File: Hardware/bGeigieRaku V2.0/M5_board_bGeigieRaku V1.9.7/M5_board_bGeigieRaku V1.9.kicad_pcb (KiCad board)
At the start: 2 copper layers, 129.4 x 64.6 mm, 27 parts, among them J1 M5 2x15 pin, J10 QI GND, J11 QI charger Plus, J2 Geiger, J3 GPS, J4 Geiger 2, J5 Extra support header, J8 QI charger GND, J9 QI Plus, Q2 IRFR9024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

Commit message: added plates
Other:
- board text added: "screws for the display are M3 12mm"
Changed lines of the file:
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@@
+    (effects (font (size 1.5 1.5) (thickness 0.3)))
+  )
+  (gr_text "screws for the display are M3 12mm" (at 107.7976 167.334) (layer "Eco2.User")
     (effects (font (size 1.5 1.5) (thickness 0.3)))
   )

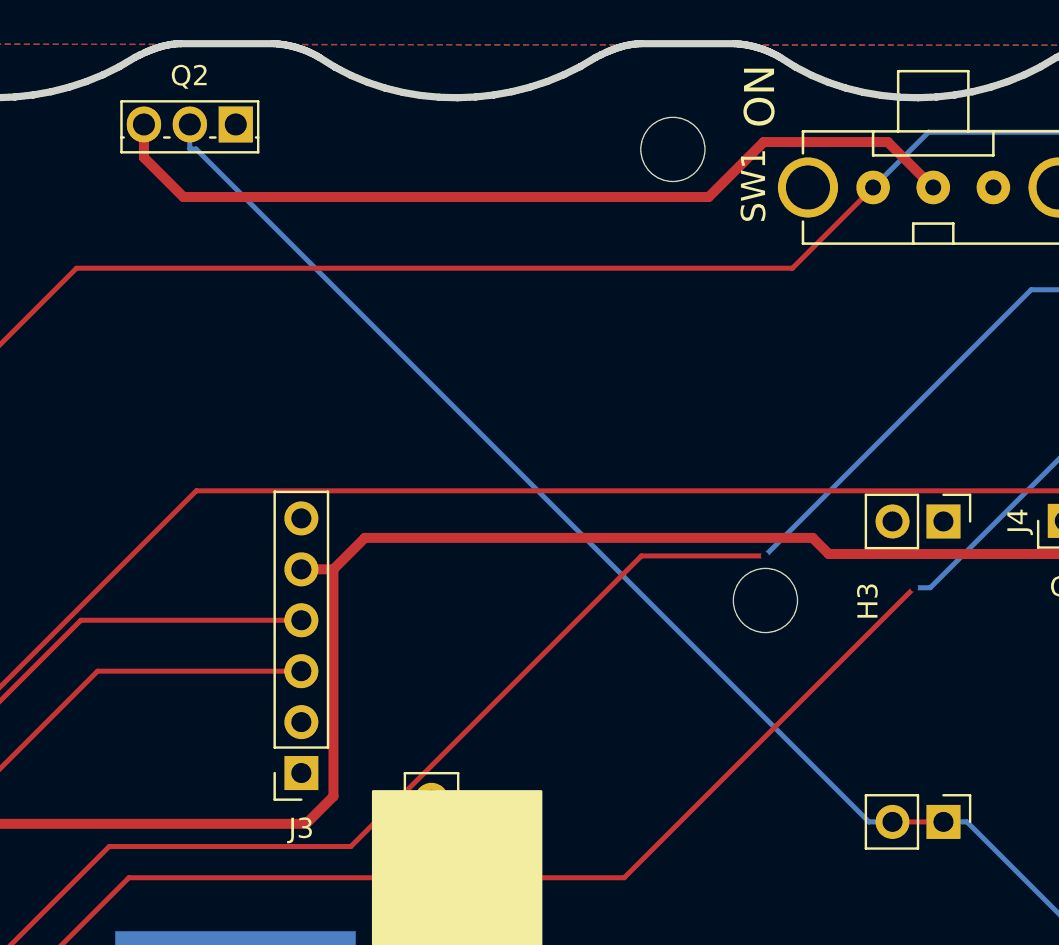
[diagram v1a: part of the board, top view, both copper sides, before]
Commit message: Adde tube rest platform
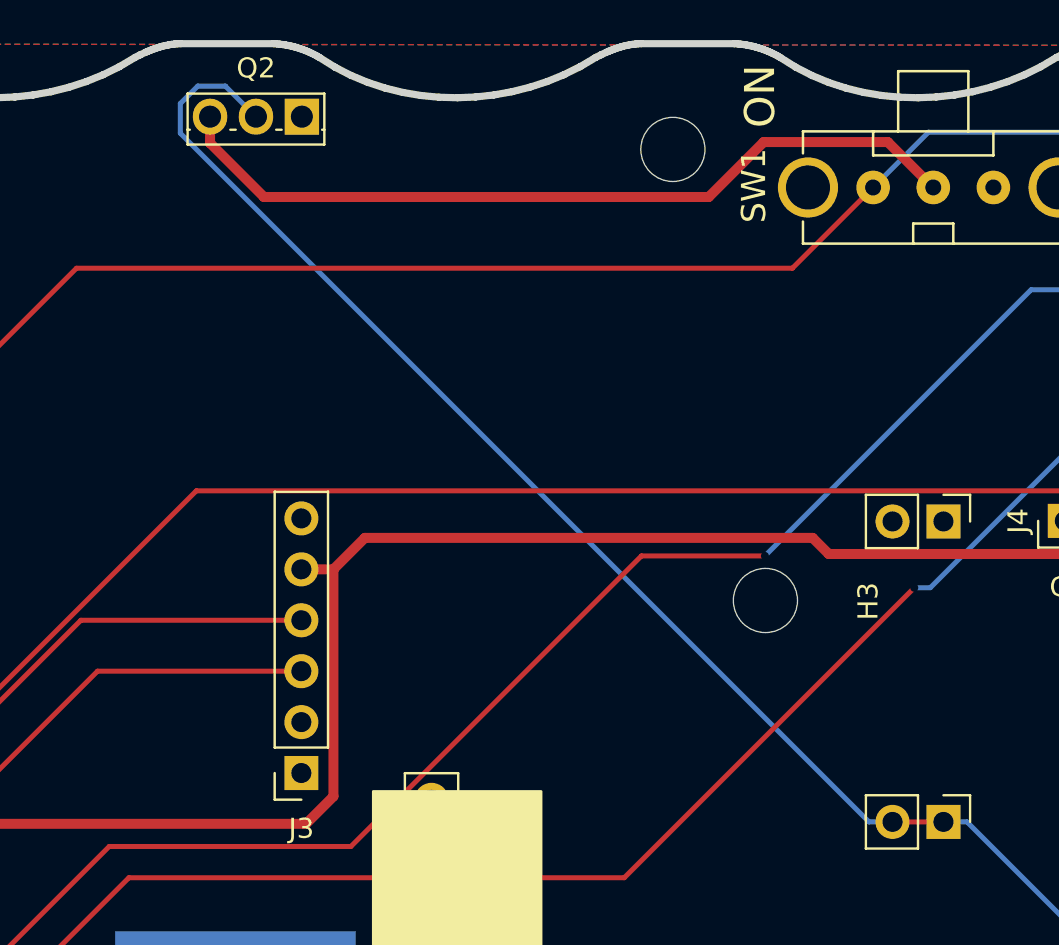
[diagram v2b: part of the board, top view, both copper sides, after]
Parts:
- moved Q2 3.32 mm to (153.0, 70.3)
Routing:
- net Net-(BT1-Pad1): track 80.5 -> 86.3 mm
- net /VBATT: track 43.9 -> 40.6 mm
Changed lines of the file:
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@@
     )
     (model "${KISYS3DMOD}/Misc.3dshapes/lnd7318-2.wrl"
-      (offset (xyz -18.5 -7 -10.5))
+      (offset (xyz -18.5 -7 -13.5))
       (scale (xyz 4 4 4))
       (rotate (xyz 90 0 -124))
     )
-    (model "/home/rob/Documents/Freecad/bGeigieZen bottom plate.x3d" hide
+    (model "/home/rob/Documents/Freecad/bGeigieZen bottom plate.x3d"
       (offset (xyz -22 15.5 -20))
       (scale (xyz 0.4 0.4 0.4))
@@
       (rotate (xyz -90 0 -90))
     )
+    (model "/home/rob/Documents/Blender/bGeigieZen_tube plate.x3d"
+      (offset (xyz -65 -139.5 -6))
+      (scale (xyz 4 4 4))
+      (rotate (xyz -90 0 -90))
+    )
   )
   (footprint "Connector_PinHeader_2.54mm:PinHeader_1x02_P2.54mm_Vertical" (layer "F.Cu")
@@
   )
   (footprint "Package_TO_SOT_THT:TO-251-3_Vertical" (layer "F.Cu")
-    (at 149.7116 70.694 180)
+    (at 153.0096 70.306 180)
     (descr "TO-251-3, Vertical, RM 2.29mm, IPAK, see https://www.diodes.com/assets/Package-Files/TO251.pdf")
     (tags "TO-251-3 Vertical RM 2.29mm IPAK")
@@
       (effects (font (size 1 1) (thickness 0.15)))
     )
-    (fp_text value "IRFR9024" (at 2.29 2.28) (layer "F.Fab")
+    (fp_text value "IRFR9024" (at 2.032 -3.048) (layer "F.Fab")
       (effects (font (size 1 1) (thickness 0.15)))
     )
@@
   (segment (start 207.108 97.87) (end 201.0076 97.87) (width 0.25) (layer "B.Cu") (net 7))
   (segment (start 201.0076 97.87) (end 193.6076 90.47) (width 0.25) (layer "B.Cu") (net 7))
-  (segment (start 145.1316 70.694) (end 145.1316 72.3444) (width 0.5) (layer "F.Cu") (net 8))
-  (segment (start 173.3056 74.313) (end 176.0456 71.573) (width 0.5) (layer "F.Cu") (net 8))
-  (segment (start 147.1002 74.313) (end 173.3056 74.313) (width 0.5) (layer "F.Cu") (net 8))
-  (segment (start 182.2406 71.573) (end 184.5056 73.838) (width 0.5) (layer "F.Cu") (net 8))
-  (segment (start 145.1316 72.3444) (end 147.1002 74.313) (width 0.5) (layer "F.Cu") (net 8))
-  (segment (start 176.0456 71.573) (end 182.2406 71.573) (width 0.5) (layer "F.Cu") (net 8))
+  (segment (start 148.4296 71.6235) (end 148.4296 70.306) (width 0.5) (layer "F.Cu") (net 8))
+  (segment (start 182.2406 71.573) (end 176.0456 71.573) (width 0.5) (layer "F.Cu") (net 8))
+  (segment (start 151.1191 74.313) (end 148.4296 71.6235) (width 0.5) (layer "F.Cu") (net 8))
+  (segment (start 184.5056 73.838) (end 182.2406 71.573) (width 0.5) (layer "F.Cu") (net 8))
+  (segment (start 173.3056 74.313) (end 151.1191 74.313) (width 0.5) (layer "F.Cu") (net 8))
+  (segment (start 176.0456 71.573) (end 173.3056 74.313) (width 0.5) (layer "F.Cu") (net 8))
   (segment (start 155.4562 106.7113) (end 143.4014 106.7113) (width 0.25) (layer "F.Cu") (net 9))
   (segment (start 136.783 115.23) (end 136.783 113.3297) (width 0.25) (layer "F.Cu") (net 9))
@@
   (segment (start 207.493 105.358) (end 210.033 105.358) (width 0.25) (layer "F.Cu") (net 10))
   (segment (start 182.474 105.485) (end 185.014 105.485) (width 0.25) (layer "F.Cu") (net 12))
+  (segment (start 150.2076 70.585687) (end 150.2076 70.56) (width 0.5) (layer "F.Cu") (net 12))
   (segment (start 197.8543 117.15) (end 186.1893 105.485) (width 0.25) (layer "B.Cu") (net 12))
-  (segment (start 147.7331 71.9194) (end 147.4216 71.9194) (width 0.25) (layer "B.Cu") (net 12))
+  (segment (start 147.81521 68.78148) (end 149.19508 68.78148) (width 0.25) (layer "B.Cu") (net 12))
   (segment (start 207.9256 117.15) (end 204.4976 117.15) (width 0.25) (layer "B.Cu") (net 12))
-  (segment (start 147.4216 70.694) (end 147.4216 71.9194) (width 0.25) (layer "B.Cu") (net 12))
+  (segment (start 146.94633 69.65036) (end 147.81521 68.78148) (width 0.25) (layer "B.Cu") (net 12))
+  (segment (start 146.94633 71.13263) (end 146.94633 69.65036) (width 0.25) (layer "B.Cu") (net 12))
+  (segment (start 182.474 105.485) (end 181.2987 105.485) (width 0.25) (layer "B.Cu") (net 12))
   (segment (start 204.4976 117.15) (end 197.8543 117.15) (width 0.25) (layer "B.Cu") (net 12))
-  (segment (start 181.2987 105.485) (end 147.7331 71.9194) (width 0.25) (layer "B.Cu") (net 12))
+  (segment (start 181.2987 105.485) (end 146.94633 71.13263) (width 0.25) (layer "B.Cu") (net 12))
+  (segment (start 149.19508 68.78148) (end 150.7196 70.306) (width 0.25) (layer "B.Cu") (net 12))
   (segment (start 185.014 105.485) (end 186.1893 105.485) (width 0.25) (layer "B.Cu") (net 12))
-  (segment (start 182.474 105.485) (end 181.2987 105.485) (width 0.25) (layer "B.Cu") (net 12))
   (segment (start 177.478 77.8656) (end 141.7671 77.8656) (width 0.25) (layer "F.Cu") (net 30))
   (segment (start 141.7671 77.8656) (end 106.303 113.3297) (width 0.25) (layer "F.Cu") (net 30))
